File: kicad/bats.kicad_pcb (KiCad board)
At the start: 2 copper layers, 28 parts, among them P1 SERVO, SW1 RESET, SW2 SHOT, SW3 UP, SW4 LEFT, SW5 DOWN, SW6 RIGHT, U1 BUZZER

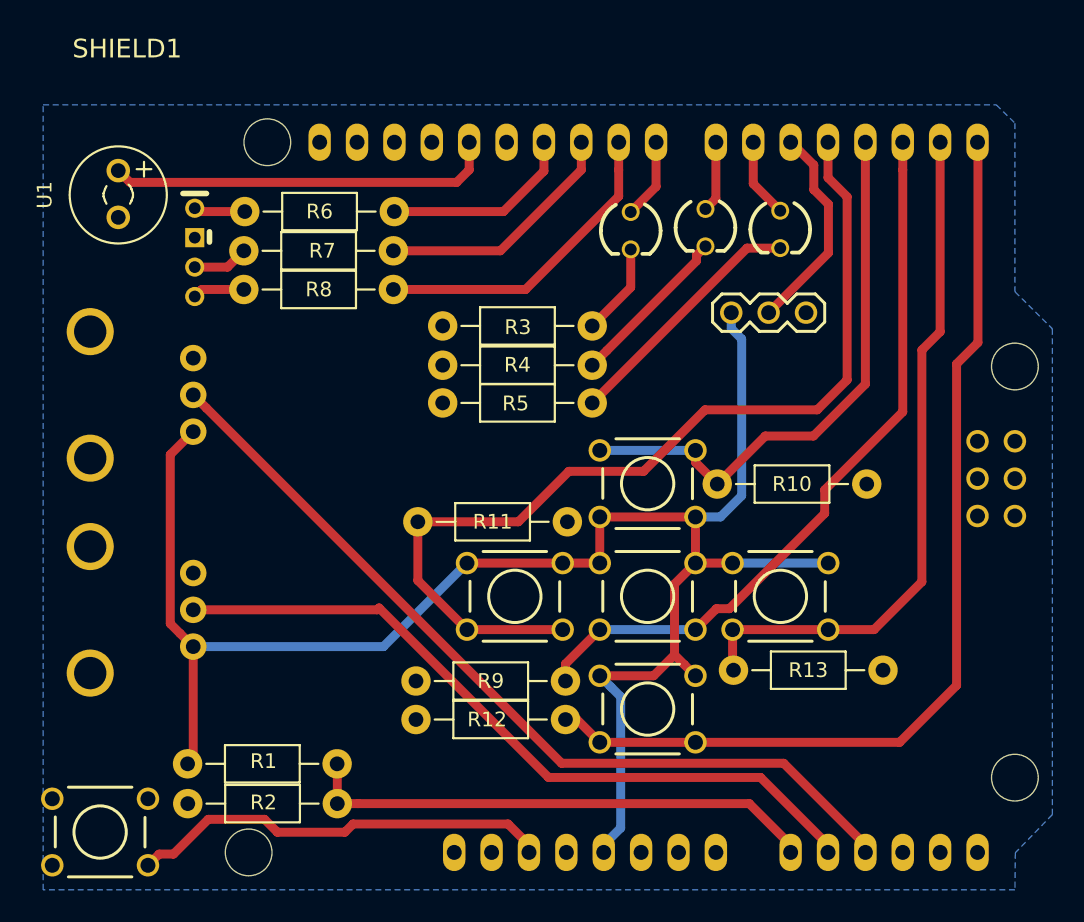
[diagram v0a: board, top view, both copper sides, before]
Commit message: Engadida area de recheo no fronte da placa
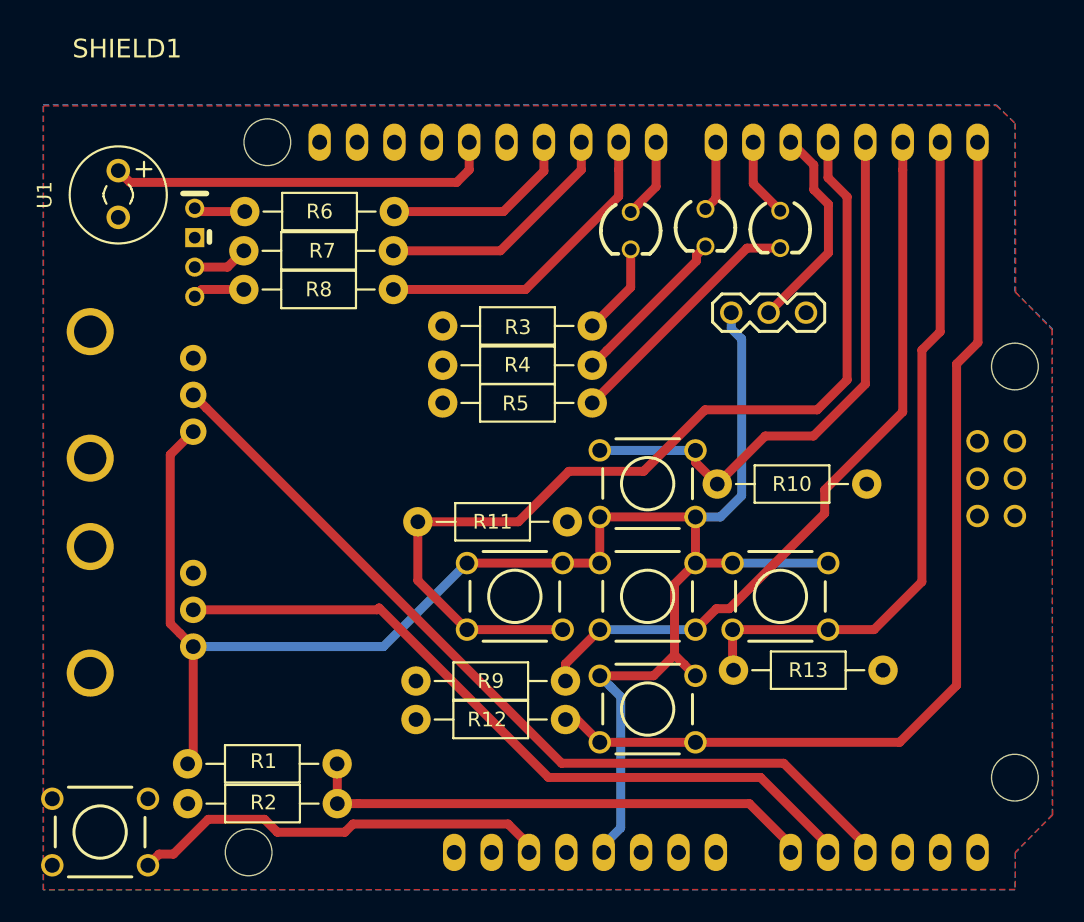
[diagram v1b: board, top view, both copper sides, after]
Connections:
- net Net-(P1-Pad1) renamed /VCC
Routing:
- added copper zone on F.Cu, net /VCC

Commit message: Correxida a forma da placa Correxida a posición do botón de reset Correxida a posición do nome da placa
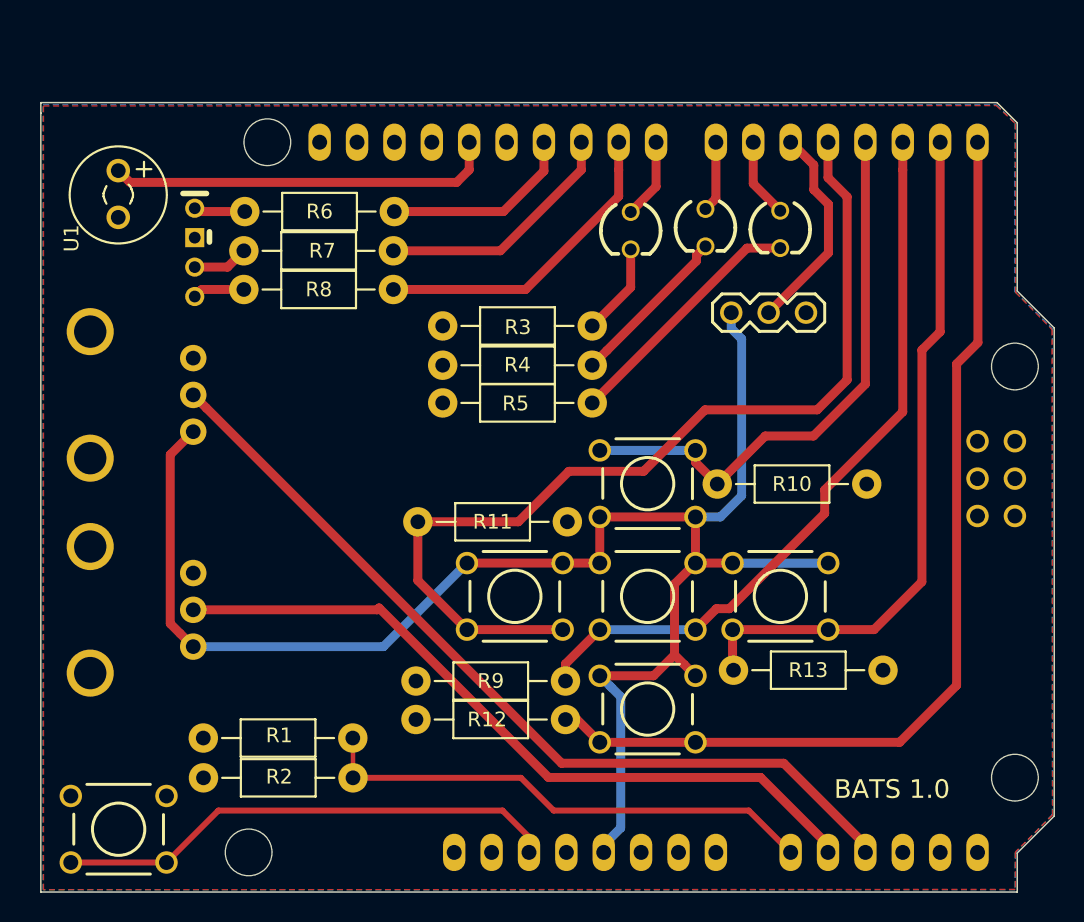
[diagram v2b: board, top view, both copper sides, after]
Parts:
- BATS 1.0: renamed from SHIELD1
- moved R1 2.05 mm to (142.9, 127.5)
- moved R2 2.05 mm to (143.0, 130.2)
- moved SW1 1.27 mm to (132.1, 133.7)
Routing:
- net /VCC: track 119.8 -> 111.7 mm
- net Net-(SHIELD1-PadRST): track 28.9 -> 34.9 mm
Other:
- board outline added: 68.9 x 53.6 mm
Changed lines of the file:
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@@
-(kicad_pcb (version 4) (host pcbnew 0.201510170916+6271~30~ubuntu14.04.1-product)
+(kicad_pcb (version 4) (host pcbnew 0.201511131146+6311~30~ubuntu14.04.1-product)
   (general
     (links 67)
-    (no_connects 1)
-    (area 124.244399 78.74 196.096701 138.3752)
+    (no_connects 0)
+    (area 126.772199 84.227199 195.731601 137.972001)
     (thickness 1.6)
-    (drawings 2)
-    (tracks 145)
+    (drawings 12)
+    (tracks 142)
     (zones 0)
     (modules 28)
@@
   )
   (setup
-    (last_trace_width 0.3048)
+    (last_trace_width 0.4064)
     (user_trace_width 0.3048)
     (user_trace_width 0.4064)
@@
     (at 126.9706 137.7696)
     (descr http://www.thingiverse.com/thing:9630)
-    (fp_text reference SHIELD1 (at 5.715 -57.15) (layer F.SilkS)
+    (fp_text reference "BATS 1.0" (at 57.6874 -6.8326) (layer F.SilkS)
       (effects (font (thickness 0.3048)))
     )
@@
     (descr "Buzzer, Elektromagnetic Beeper, Summer,")
     (tags "Kingstate, KCG0601,")
-    (fp_text reference U1 (at 1.524 -5.00126 90) (layer F.SilkS)
+    (fp_text reference U1 (at -1.4224 -3.175 90) (layer F.SilkS)
       (effects (font (size 1 1) (thickness 0.15)))
     )
@@
   )
   (module Resistors_ThroughHole:Resistor_Horizontal_RM10mm (layer F.Cu)
-    (at 141.8717 129.2098)
+    (at 142.9385 127.4572)
     (descr "Resistor, Axial,  RM 10mm, 1/3W,")
     (tags "Resistor, Axial, RM 10mm, 1/3W,")
@@
   )
   (module FT:SW_PUSHBUTTON_PTH (layer F.Cu)
-    (at 130.8481 133.8453)
+    (at 132.1054 133.6548)
     (descr "<b>OMRON SWITCH</b>")
     (fp_text reference SW1 (at -0.05 0) (layer Eco1.User)
@@
   )
   (module Resistors_ThroughHole:Resistor_Horizontal_RM10mm (layer F.Cu)
-    (at 141.8844 131.9149 180)
+    (at 142.9512 130.1623 180)
     (descr "Resistor, Axial,  RM 10mm, 1/3W,")
     (tags "Resistor, Axial, RM 10mm, 1/3W,")
@@
       (net 20 /ARD1))
   )
+  (gr_line (start 126.8222 137.922) (end 126.8222 84.9884) (angle 90) (layer Edge.Cuts) (width 0.1))
+  (gr_line (start 193.167 137.922) (end 126.8222 137.922) (angle 90) (layer Edge.Cuts) (width 0.1))
+  (gr_line (start 193.167 135.2804) (end 193.167 137.922) (angle 90) (layer Edge.Cuts) (width 0.1))
+  (gr_line (start 195.6816 132.7658) (end 193.167 135.2804) (angle 90) (layer Edge.Cuts) (width 0.1))
+  (gr_line (start 195.6816 99.5934) (end 195.6816 132.7658) (angle 90) (layer Edge.Cuts) (width 0.1))
+  (gr_line (start 193.167 97.0788) (end 195.6816 99.5934) (angle 90) (layer Edge.Cuts) (width 0.1))
+  (gr_line (start 193.167 85.6488) (end 193.167 97.0788) (angle 90) (layer Edge.Cuts) (width 0.1))
+  (gr_line (start 191.7954 84.2772) (end 193.167 85.6488) (angle 90) (layer Edge.Cuts) (width 0.1))
+  (gr_line (start 126.8222 84.2772) (end 191.7954 84.2772) (angle 90) (layer Edge.Cuts) (width 0.1))
+  (gr_line (start 126.8222 84.9884) (end 126.8222 84.2772) (angle 90) (layer Edge.Cuts) (width 0.1))
   (target plus (at 192.7352 124.6886) (size 5) (width 0.1) (layer Edge.Cuts))
   (target plus (at 133.477 96.5454) (size 5) (width 0.1) (layer Edge.Cuts))
@@
   (segment (start 162.206701 129.171701) (end 138.074999 105.039999) (width 0.6096) (layer F.Cu) (net 9))
   (segment (start 138.074999 105.039999) (end 137.175 104.14) (width 0.6096) (layer F.Cu) (net 9))
+  (segment (start 159.9906 135.2296) (end 159.9906 134.1842) (width 0.4064) (layer F.Cu) (net 10))
+  (segment (start 159.9906 134.1842) (end 158.1912 132.3848) (width 0.4064) (layer F.Cu) (net 10))
+  (segment (start 138.8872 132.3848) (end 135.3566 135.9154) (width 0.4064) (layer F.Cu) (net 10))
+  (segment (start 158.1912 132.3848) (end 138.8872 132.3848) (width 0.4064) (layer F.Cu) (net 10))
+  (segment (start 135.3566 135.9154) (end 128.8542 135.9154) (width 0.4064) (layer F.Cu) (net 10))
   (segment (start 159.9906 135.2296) (end 159.9906 134.7216) (width 0.6096) (layer F.Cu) (net 10))
-  (segment (start 159.9906 134.7216) (end 158.56819 133.29919) (width 0.6096) (layer F.Cu) (net 10))
-  (segment (start 158.56819 133.29919) (end 148.03675 133.29919) (width 0.6096) (layer F.Cu) (net 10))
-  (segment (start 142.895894 133.858) (end 142.019593 132.981699) (width 0.6096) (layer F.Cu) (net 10))
-  (segment (start 148.03675 133.29919) (end 147.47794 133.858) (width 0.6096) (layer F.Cu) (net 10))
-  (segment (start 147.47794 133.858) (end 142.895894 133.858) (width 0.6096) (layer F.Cu) (net 10))
-  (segment (start 142.019593 132.981699) (end 138.194241 132.981699) (width 0.6096) (layer F.Cu) (net 10))
-  (segment (start 138.194241 132.981699) (end 135.832039 135.343901) (width 0.6096) (layer F.Cu) (net 10))
-  (segment (start 135.832039 135.343901) (end 134.861299 135.343901) (width 0.6096) (layer F.Cu) (net 10))
-  (segment (start 134.861299 135.343901) (end 134.0993 136.1059) (width 0.6096) (layer F.Cu) (net 10))
   (segment (start 158.2547 91.6813) (end 161.0066 88.9294) (width 0.6096) (layer F.Cu) (net 11))
   (segment (start 161.0066 88.9294) (end 161.0066 86.9696) (width 0.6096) (layer F.Cu) (net 11))
@@
   (segment (start 181.61 103.124) (end 181.61 90.678) (width 0.6096) (layer F.Cu) (net 23))
   (segment (start 181.61 90.678) (end 180.3106 89.3786) (width 0.6096) (layer F.Cu) (net 23))
-  (segment (start 146.9644 131.9149) (end 146.9644 129.2225) (width 0.6096) (layer F.Cu) (net 24))
-  (segment (start 146.9644 129.2225) (end 146.9517 129.2098) (width 0.6096) (layer F.Cu) (net 24))
+  (segment (start 148.0312 130.1623) (end 159.4485 130.1623) (width 0.4064) (layer F.Cu) (net 24))
+  (segment (start 174.9258 132.3848) (end 177.7706 135.2296) (width 0.4064) (layer F.Cu) (net 24))
+  (segment (start 161.671 132.3848) (end 174.9258 132.3848) (width 0.4064) (layer F.Cu) (net 24))
+  (segment (start 159.4485 130.1623) (end 161.671 132.3848) (width 0.4064) (layer F.Cu) (net 24))
+  (segment (start 177.7706 135.2296) (end 177.7706 134.7684) (width 0.4064) (layer F.Cu) (net 24))
+  (segment (start 177.7706 135.2296) (end 177.7706 135.1748) (width 0.3048) (layer F.Cu) (net 24))
+  (segment (start 148.0312 130.1623) (end 148.0312 127.4699) (width 0.3048) (layer F.Cu) (net 24))
+  (segment (start 148.0312 127.4699) (end 148.0185 127.4572) (width 0.3048) (layer F.Cu) (net 24))
   (segment (start 177.7706 135.2296) (end 177.7706 134.7216) (width 0.6096) (layer F.Cu) (net 24))
-  (segment (start 177.7706 134.7216) (end 174.9639 131.9149) (width 0.6096) (layer F.Cu) (net 24))
-  (segment (start 174.9639 131.9149) (end 148.377892 131.9149) (width 0.6096) (layer F.Cu) (net 24))
-  (segment (start 148.377892 131.9149) (end 146.9644 131.9149) (width 0.6096) (layer F.Cu) (net 24))
   (segment (start 171.30395 112.4331) (end 173.00494 112.4331) (width 0.6096) (layer B.Cu) (net 42))
   (segment (start 173.00494 112.4331) (end 174.443391 110.994649) (width 0.6096) (layer B.Cu) (net 42))
@@
   (segment (start 155.7782 115.57) (end 150.1032 121.245) (width 0.6096) (layer B.Cu) (net 42))
   (segment (start 150.1032 121.245) (end 137.175 121.245) (width 0.6096) (layer B.Cu) (net 42))
-  (segment (start 137.175 121.245) (end 137.175 128.8265) (width 0.6096) (layer F.Cu) (net 42))
-  (segment (start 137.175 128.8265) (end 136.7917 129.2098) (width 0.6096) (layer F.Cu) (net 42))
   (segment (start 137.175 106.64) (end 135.614599 108.200401) (width 0.6096) (layer F.Cu) (net 42))
   (segment (start 135.614599 108.200401) (end 135.614599 119.684599) (width 0.6096) (layer F.Cu) (net 42))

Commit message: Engadidos Silks de probas Limpeza de directorios Exportados Gerber
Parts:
- added BATS v 1.0: Symbol_OSHW-Logo_SilkScreen, Symbols:Symbol_OSHW-Logo_SilkScreen, F.Cu at (147.4, 105.7)
- added G***: LOGO, silklibrary:bat_b, B.Cu at (162.4, 120.0)
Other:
- board text added: "by BricoLabs"
